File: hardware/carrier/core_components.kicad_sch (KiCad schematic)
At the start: 58 parts, among them J3 PANEL, J4 CARDKB, J6 EXT_LED, J7 HAPTIC, J8 PIEZ, M1 Walter, Q3 MMBT3904, Q4 AO3400A, Q5 UMH3N, SW2 SKQGAFE010, U11 SN74LVC2G126DCUR, U7 LIS2DW12TR, U8 CP2102N-A02-GQFN24, U9 DRV2605LDGSR

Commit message: Move sheets property to top level
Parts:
- removed C12, C13: 100uF, Capacitor_SMD:C_0805_2012Metric, symbol Device:C
- removed C14, C20, C22, C23: 10uF, Capacitor_SMD:C_0603_1608Metric, symbol Device:C
- removed C21, C24, C26, C29, C30, C32: 100nF, Capacitor_SMD:C_0603_1608Metric, symbol Device:C
- removed C25, C27: 1uF, Capacitor_SMD:C_0603_1608Metric, symbol Device:C
- removed C28, C31: 4.7uF, Capacitor_SMD:C_0603_1608Metric, symbol Device:C
- removed J3: PANEL, Connector_JST:JST_SH_SM10B-SRSS-TB_1x10-1MP_P1.00mm_Horizontal, symbol Connector_Generic:Conn_01x10
- removed J4: CARDKB, Connector_JST:JST_PH_S4B-PH-SM4-TB_1x04-1MP_P2.00mm_Horizontal, symbol Connector_Generic:Conn_01x04
- removed J6: EXT_LED, Connector_JST:JST_SH_SM02B-SRSS-TB_1x02-1MP_P1.00mm_Horizontal, symbol Connector_Generic:Conn_01x02
- removed J7: HAPTIC, Connector_JST:JST_SH_SM02B-SRSS-TB_1x02-1MP_P1.00mm_Horizontal, symbol Connector_Generic:Conn_01x02
- removed J8: PIEZ, Connector_JST:JST_SH_SM02B-SRSS-TB_1x02-1MP_P1.00mm_Horizontal, symbol Connector_Generic:Conn_01x02
- removed JP2: auto-boot, Jumper:SolderJumper-2_P1.3mm_Bridged_RoundedPad1.0x1.5mm, symbol Jumper:SolderJumper_2_Bridged
- removed M1: Walter, pager-carrier:Walter_Module_2x14_THT, symbol pager-carrier:Walter
- removed Q3: MMBT3904, Package_TO_SOT_SMD:SOT-23, symbol Transistor_BJT:MMBT3904
- removed Q4: AO3400A, Package_TO_SOT_SMD:SOT-23, symbol Transistor_FET:AO3400A
- removed Q5: UMH3N, Package_TO_SOT_SMD:SOT-363_SC-70-6, symbol Transistor_BJT:UMH3N
- removed R20: 0R, Resistor_SMD:R_0603_1608Metric, symbol Device:R
- removed R29, R30, R31, R32: 4.7k, Resistor_SMD:R_0603_1608Metric, symbol Device:R
- removed R33: 0R, Resistor_SMD:R_1206_3216Metric, symbol Device:R
- removed R34, R43: 1k, Resistor_SMD:R_0603_1608Metric, symbol Device:R
- removed R35, R36, R44, R45: 100k, Resistor_SMD:R_0603_1608Metric, symbol Device:R
- removed R37: 330R, Resistor_SMD:R_0603_1608Metric, symbol Device:R
- removed R38, R39: 220R, Resistor_SMD:R_0603_1608Metric, symbol Device:R
- removed R40: 15R, Resistor_SMD:R_0603_1608Metric, symbol Device:R
- removed R41: 22.1k, Resistor_SMD:R_0603_1608Metric, symbol Device:R
- removed R42: 47.5k, Resistor_SMD:R_0603_1608Metric, symbol Device:R
- removed R46, R47, R48: 10k, Resistor_SMD:R_0603_1608Metric, symbol Device:R
- removed R49: 1M, Resistor_SMD:R_0603_1608Metric, symbol Device:R
- removed SW2: SKQGAFE010, Button_Switch_SMD:SW_SPST_SKQG_WithoutStem, symbol Switch:SW_Push
- removed TP10: FL_BTN, TestPoint:TestPoint_Pad_1.0x1.0mm, symbol Connector:TestPoint
- removed TP11: 3V3_AWK, TestPoint:TestPoint_Pad_1.0x1.0mm, symbol Connector:TestPoint
- removed TP7: AWK_EN_N, TestPoint:TestPoint_Pad_1.0x1.0mm, symbol Connector:TestPoint
- removed TP8: TP_IO1, TestPoint:TestPoint_Pad_1.0x1.0mm, symbol Connector:TestPoint
- removed TP9: TP_IO5, TestPoint:TestPoint_Pad_1.0x1.0mm, symbol Connector:TestPoint
- removed U11: SN74LVC2G126DCUR, Package_SO:VSSOP-8_2.3x2mm_P0.5mm, symbol 74xGxx:74LVC2G126
- removed U7: LIS2DW12TR, Package_LGA:LGA-12_2x2mm_P0.5mm, symbol pager-carrier:LIS2DW12TR
- removed U8: CP2102N-A02-GQFN24, Package_DFN_QFN:QFN-24-1EP_4x4mm_P0.5mm_EP2.6x2.6mm, symbol Interface_USB:CP2102N-Axx-xQFN24
- removed U9: DRV2605LDGSR, Package_SO:TSSOP-10_3x3mm_P0.5mm, symbol pager-carrier:DRV2605LDGSR
- added C15, C16: 100uF, Capacitor_SMD:C_0805_2012Metric, symbol Device:C
- added C17, C38, C40, C43: 10uF, Capacitor_SMD:C_0603_1608Metric, symbol Device:C
- added C33, C36: 4.7uF, Capacitor_SMD:C_0603_1608Metric, symbol Device:C
- added C34, C35, C37, C39, C42, C45: 100nF, Capacitor_SMD:C_0603_1608Metric, symbol Device:C
- added C41, C44: 1uF, Capacitor_SMD:C_0603_1608Metric, symbol Device:C
- added J10: HAPTIC, Connector_JST:JST_SH_SM02B-SRSS-TB_1x02-1MP_P1.00mm_Horizontal, symbol Connector_Generic:Conn_01x02
- added J11: EXT_LED, Connector_JST:JST_SH_SM02B-SRSS-TB_1x02-1MP_P1.00mm_Horizontal, symbol Connector_Generic:Conn_01x02
- added J12: PIEZ, Connector_JST:JST_SH_SM02B-SRSS-TB_1x02-1MP_P1.00mm_Horizontal, symbol Connector_Generic:Conn_01x02
- added J5: PANEL, Connector_JST:JST_SH_SM10B-SRSS-TB_1x10-1MP_P1.00mm_Horizontal, symbol Connector_Generic:Conn_01x10
- added J9: CARDKB, Connector_JST:JST_PH_S4B-PH-SM4-TB_1x04-1MP_P2.00mm_Horizontal, symbol Connector_Generic:Conn_01x04
- added JP3: auto-boot, Jumper:SolderJumper-2_P1.3mm_Bridged_RoundedPad1.0x1.5mm, symbol Jumper:SolderJumper_2_Bridged
- added M2: Walter, pager-carrier:Walter_Module_2x14_THT, symbol pager-carrier:Walter
- added Q6: UMH3N, Package_TO_SOT_SMD:SOT-363_SC-70-6, symbol Transistor_BJT:UMH3N
- added Q7: AO3400A, Package_TO_SOT_SMD:SOT-23, symbol Transistor_FET:AO3400A
- added Q8: MMBT3904, Package_TO_SOT_SMD:SOT-23, symbol Transistor_BJT:MMBT3904
- added R21: 0R, Resistor_SMD:R_0603_1608Metric, symbol Device:R
- added R50: 22.1k, Resistor_SMD:R_0603_1608Metric, symbol Device:R
- added R51: 47.5k, Resistor_SMD:R_0603_1608Metric, symbol Device:R
- added R52, R58: 1k, Resistor_SMD:R_0603_1608Metric, symbol Device:R
- added R53, R54, R55, R59: 100k, Resistor_SMD:R_0603_1608Metric, symbol Device:R
- added R56, R57, R62: 10k, Resistor_SMD:R_0603_1608Metric, symbol Device:R
- added R60: 15R, Resistor_SMD:R_0603_1608Metric, symbol Device:R
- added R61: 0R, Resistor_SMD:R_1206_3216Metric, symbol Device:R
- added R63, R64, R65, R66: 4.7k, Resistor_SMD:R_0603_1608Metric, symbol Device:R
- added R67, R68: 220R, Resistor_SMD:R_0603_1608Metric, symbol Device:R
- added R69: 330R, Resistor_SMD:R_0603_1608Metric, symbol Device:R
- added R70: 1M, Resistor_SMD:R_0603_1608Metric, symbol Device:R
- added SW3: SKQGAFE010, Button_Switch_SMD:SW_SPST_SKQG_WithoutStem, symbol Switch:SW_Push
- added TP12: AWK_EN_N, TestPoint:TestPoint_Pad_1.0x1.0mm, symbol Connector:TestPoint
- added TP13: TP_IO1, TestPoint:TestPoint_Pad_1.0x1.0mm, symbol Connector:TestPoint
- added TP14: TP_IO5, TestPoint:TestPoint_Pad_1.0x1.0mm, symbol Connector:TestPoint
- added TP15: FL_BTN, TestPoint:TestPoint_Pad_1.0x1.0mm, symbol Connector:TestPoint
- added TP16: 3V3_AWK, TestPoint:TestPoint_Pad_1.0x1.0mm, symbol Connector:TestPoint
- added U12: CP2102N-A02-GQFN24, Package_DFN_QFN:QFN-24-1EP_4x4mm_P0.5mm_EP2.6x2.6mm, symbol Interface_USB:CP2102N-Axx-xQFN24
- added U13: SN74LVC2G126DCUR, Package_SO:VSSOP-8_2.3x2mm_P0.5mm, symbol 74xGxx:74LVC2G126
- added U14: DRV2605LDGSR, Package_SO:TSSOP-10_3x3mm_P0.5mm, symbol pager-carrier:DRV2605LDGSR
- added U15: LIS2DW12TR, Package_LGA:LGA-12_2x2mm_P0.5mm, symbol pager-carrier:LIS2DW12TR
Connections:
- net 3V3: now also C38.1, C42.1, C43.1, R21.1, R54.2, R62.2, R65.1, R66.1, U15.10 (VDD_IO), U15.2 (CS), U15.9 (VDD)
- net 3V3_AWK: now also C40.1, C44.1, C45.1, J9.3 (Pin_3), M2.26 (3V3_OUT), R63.1, R64.1, TP16.1, U14.10 (VDD), U14.5 (EN), U14.6 (VDD/NC)
- net ACC_INT1: now also M2.20 (IO16), U15.12 (INT1)
- net AON_SCL: now also M2.22 (IO18), R66.2, U15.1 (SCL/SPC)
- net AON_SDA: now also M2.21 (IO17), R65.2, U15.4 (SDA/SDI/SDO)
- net AWK_EN_N: now also JP3.2 (B), M2.4 (DFU/3V3_EN), TP12.1
- net AWK_SCL: now also J9.1 (Pin_1), M2.24 (IO9), R64.2, U14.2 (SCL)
- net AWK_SDA: now also J9.2 (Pin_2), M2.25 (IO10), R63.2, U14.3 (SDA)
- net BRG_3V3: now also C35.2, C36.2, C39.1, R52.2, U12.5 (VIO), U12.6 (VDD), U13.8 (VCC)
- net BRG_RXD: now also U12.20 (RXD), U13.6
- net BRG_TXD: now also U12.21 (TXD), U13.5
- net CHG_STAT1: now also M2.8 (IO38)
- net CHG_STAT2: now also M2.12 (IO42)
- net EINK_BUSY: now also J5.8 (Pin_8), M2.6 (IO11)
- net EINK_CS: now also J5.5 (Pin_5), M2.10 (IO40)
- net EINK_DC: now also J5.6 (Pin_6), M2.9 (IO39)
- net EINK_MOSI: now also J5.4 (Pin_4), M2.11 (IO41)
- net EINK_RST: now also J5.7 (Pin_7), M2.7 (IO13)
- net EINK_SCK: now also J5.3 (Pin_3), M2.13 (IO2)
- net ESP_EN: now also M2.1 (RESET), Q6.6 (C1)
- net ESP_RX0: now also M2.2 (IO44/RX0), R62.1, U13.3
- net ESP_TX0: now also M2.3 (IO43/TX0), U13.2
- net EXT_LED: now also M2.23 (IO8), R69.1
- net FL_BTN: now also C37.1, M2.15 (IO4), R54.1, SW3.1, TP15.1
- net FL_N: now also J5.10 (Pin_10), Q7.3 (D)
- net FL_P: now also J5.9 (Pin_9), R61.1
- net FL_PWM: now also M2.18 (IO7), R58.1
- net GND: now also C15.2, C16.2, C17.2, C33.2, C34.2, C35.1, C36.1, C37.2, C38.2, C39.2, C40.2, C41.2, C42.2, C43.2, C44.2, C45.2, J11.2 (Pin_2), J5.2 (Pin_2), J9.4 (Pin_4), M2.27 (GND), Q8.2 (E), R51.2, R53.2, R55.2, R59.2, R60.2, SW3.2, U12.18 (~{CTS}), U12.2 (GND), U12.25 (GND), U13.4 (GND), U14.4 (IN/TRIG), U14.8 (GND), U15.3 (SDO/SA0), U15.6 (GND), U15.7 (RES), U15.8 (GND)
- net PIEZ_N: now also M2.5 (IO12), R68.1
- net PIEZ_P: now also M2.17 (IO6), R67.1
- net SYS_SW: now also C15.1, C16.1, C17.1, M2.28 (VIN), R61.2
- net TP_IO1: now also M2.14 (IO1), TP13.1
- net TP_IO5: now also M2.16 (IO5), TP14.1
- net USB_DM: now also U12.4 (D-)
- net USB_DP: now also U12.3 (D+)
- net VBUS: now also C33.1, C34.1, R50.1, U12.7 (VREGIN)
- net VBUS_DET: now also M2.19 (IO15), U13.1, U13.7
- new net: J5.1 (Pin_1), R21.2
- new net: Q7.1 (G), Q8.3 (C), R58.2, R59.1
- new net: R50.2, R51.1, U12.8 (VBUS)
- new net: J12.1 (Pin_1), R67.2, R70.2
- new net: C41.1, U14.1 (REG)
- new net: JP3.1 (A), Q6.3 (C2)
- new net: Q6.4 (E2), R55.1, R56.1, U12.23 (~{DTR})
- new net: Q6.5 (B2), R57.2
- new net: J11.1 (Pin_1), R69.2
- new net: Q7.2 (S), Q8.1 (B), R60.1
- new net: Q6.1 (E1), R53.1, R57.1, U12.19 (~{RTS})
- new net: R52.1, U12.9 (~{RST})
- new net: J12.2 (Pin_2), R68.2, R70.1
- new net: J10.1 (Pin_1), U14.7 (OUT+)
- new net: J10.2 (Pin_2), U14.9 (OUT-)
- new net: Q6.2 (B1), R56.2
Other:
- company: awong-dev/pager -> (none)
- title: Walter module header, bulk capacitance, test pads, mounting holes -> (none)

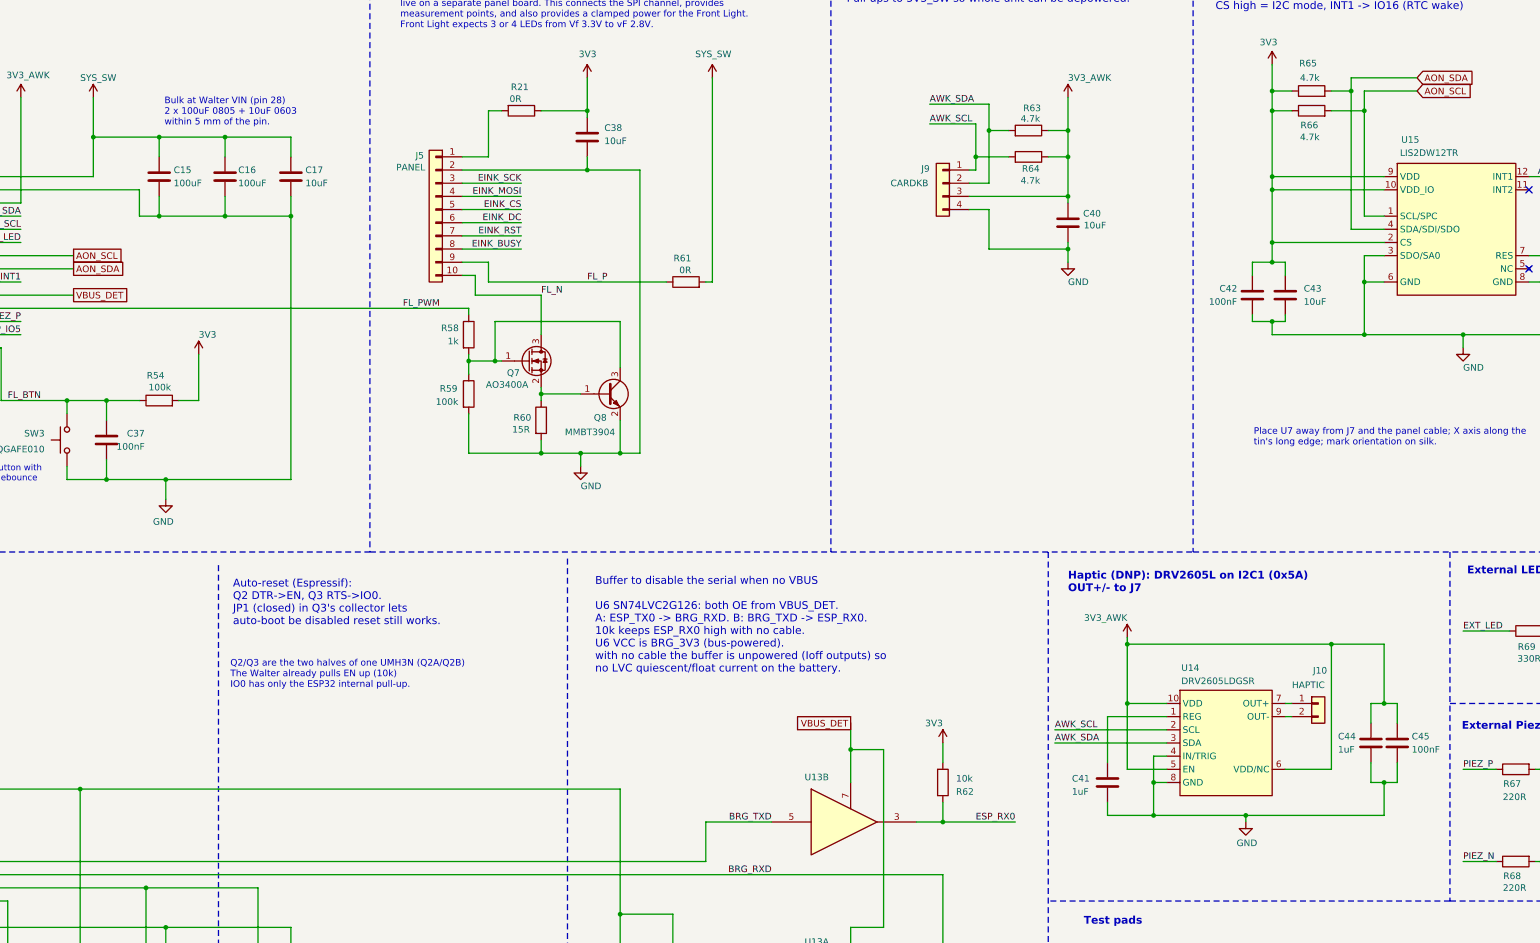
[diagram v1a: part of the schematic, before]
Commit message: Remove unnecessary caps and shrink some components
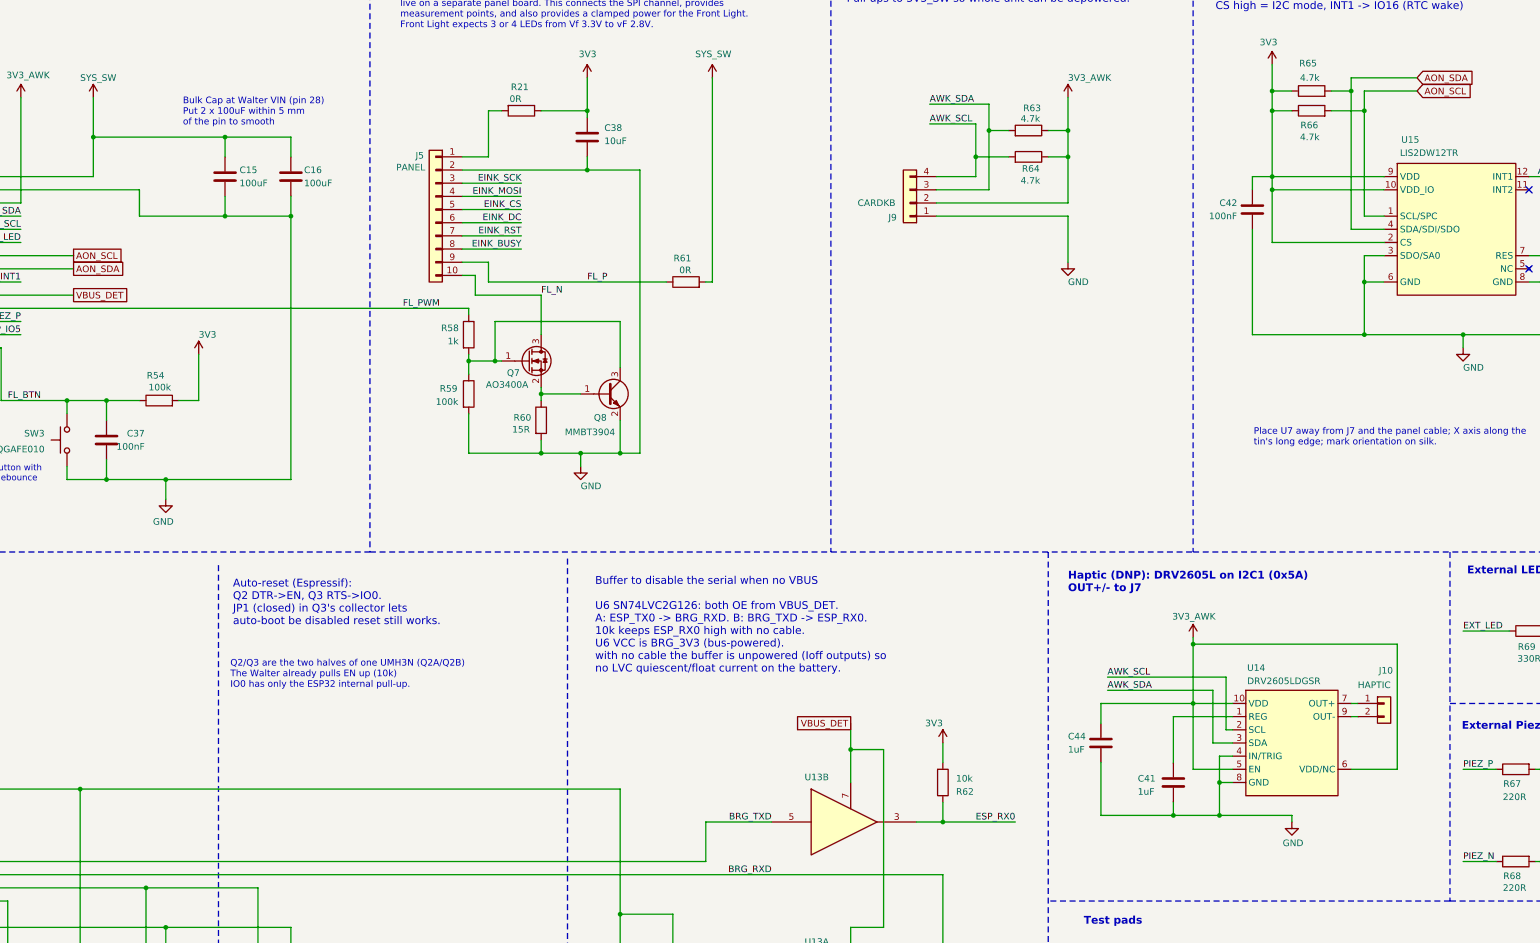
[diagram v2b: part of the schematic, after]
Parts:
- removed C17, C40, C43: 10uF, Capacitor_SMD:C_0603_1608Metric, symbol Device:C
- removed C45: 100nF, Capacitor_SMD:C_0603_1608Metric, symbol Device:C
- J9: footprint Connector_JST:JST_PH_S4B-PH-SM4-TB_1x04-1MP_P2.00mm_Horizontal -> Connector_JST:JST_SH_SM04B-SRSS-TB_1x04-1MP_P1.00mm_Horizontal
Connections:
- net 3V3_AWK: now also J9.2 (Pin_2); no longer J9.3 (Pin_3)
- net AWK_SCL: now also J9.4 (Pin_4); no longer J9.1 (Pin_1)
- net AWK_SDA: now also J9.3 (Pin_3); no longer J9.2 (Pin_2)
- net GND: now also J9.1 (Pin_1); no longer J9.4 (Pin_4)
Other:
- note added: "Bulk Cap at Walter VIN (pin 28) Put 2 x 100uF within 5 mm of the pin to smooth"
- note removed: "Bulk at Walter VIN (pin 28) 2 x 100uF 0805 + 10uF 0603 within 5 mm of the pin."
- moved on the sheet: C15, C16, C41, C42, C44, J10, J9, U14

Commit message: AI resized many of the components
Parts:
- C34, C35, C37, C39, C42: footprint Capacitor_SMD:C_0603_1608Metric -> Capacitor_SMD:C_0402_1005Metric; LCSC C14663 -> C1525; MPN CL10B104KB8NNNC -> CL05B104KO5NNNC
- C36: footprint Capacitor_SMD:C_0603_1608Metric -> Capacitor_SMD:C_0402_1005Metric; LCSC C19666 -> C23733; MPN CL10A475KP8NNNC -> CL05A475MP5NRNC
- C41, C44: footprint Capacitor_SMD:C_0603_1608Metric -> Capacitor_SMD:C_0402_1005Metric; LCSC C15849 -> C52923; MPN CL10A105KA8NNNC -> CL05A105KA5NQNC
- Q7: value AO3400A -> SI1308EDL; footprint Package_TO_SOT_SMD:SOT-23 -> Package_TO_SOT_SMD:SOT-323_SC-70; LCSC C20917 -> C469327; MPN AO3400A -> SI1308EDL-T1-GE3
- Q8: value MMBT3904 -> MMST3904; footprint Package_TO_SOT_SMD:SOT-23 -> Package_TO_SOT_SMD:SOT-323_SC-70; LCSC C20526 -> C54879; MPN MMBT3904 -> MMST3904
- R21: footprint Resistor_SMD:R_0603_1608Metric -> Resistor_SMD:R_0402_1005Metric; LCSC C21189 -> C17168; MPN 0603WAF0000T5E -> 0402WGF0000TCE
- R50: footprint Resistor_SMD:R_0603_1608Metric -> Resistor_SMD:R_0402_1005Metric; LCSC C137768 -> C43473; MPN RC0603FR-0722K1L -> 0402WGF2212TCE
- R51: footprint Resistor_SMD:R_0603_1608Metric -> Resistor_SMD:R_0402_1005Metric; LCSC C23061 -> C25896; MPN 0603WAF4752T5E -> 0402WGF4752TCE
- R52, R58: footprint Resistor_SMD:R_0603_1608Metric -> Resistor_SMD:R_0402_1005Metric; LCSC C21190 -> C11702; MPN 0603WAF1001T5E -> 0402WGF1001TCE
- R53, R54, R55, R59: footprint Resistor_SMD:R_0603_1608Metric -> Resistor_SMD:R_0402_1005Metric; LCSC C25803 -> C25741; MPN 0603WAF1003T5E -> 0402WGF1003TCE
- R56, R57, R62: footprint Resistor_SMD:R_0603_1608Metric -> Resistor_SMD:R_0402_1005Metric; LCSC C25804 -> C25744; MPN 0603WAF1002T5E -> 0402WGF1002TCE
- R61: footprint Resistor_SMD:R_1206_3216Metric -> Resistor_SMD:R_0402_1005Metric; LCSC C17888 -> C17168; MPN 1206W4F0000T5E -> 0402WGF0000TCE
- R63, R64, R65, R66: footprint Resistor_SMD:R_0603_1608Metric -> Resistor_SMD:R_0402_1005Metric; LCSC C23162 -> C25900; MPN 0603WAF4701T5E -> 0402WGF4701TCE
- R67, R68: footprint Resistor_SMD:R_0603_1608Metric -> Resistor_SMD:R_0402_1005Metric; LCSC C22962 -> C25091; MPN 0603WAF2200T5E -> 0402WGF2200TCE
- R69: footprint Resistor_SMD:R_0603_1608Metric -> Resistor_SMD:R_0402_1005Metric; LCSC C23138 -> C25104; MPN 0603WAF3300T5E -> 0402WGF3300TCE
- R70: footprint Resistor_SMD:R_0603_1608Metric -> Resistor_SMD:R_0402_1005Metric; LCSC C22935 -> C26083; MPN 0603WAF1004T5E -> 0402WGF1004TCE

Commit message: components renumbered
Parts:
- renumbered C33 to C1, C44 to C10, C41 to C11, C42 to C12, C34 to C2, C35 to C3, C36 to C4, C37 to C5, C15 to C6, C16 to C7, C38 to C8, C39 to C9, J5 to J1, J9 to J2, J10 to J3, J11 to J4, J12 to J5, JP3 to JP1, M2 to M1, Q6 to Q1, Q7 to Q2, Q8 to Q3, R50 to R1, R59 to R10, R21 to R11, R60 to R12, R61 to R13, R62 to R14, R63 to R15, R64 to R16, R65 to R17, R66 to R18, R67 to R19, R51 to R2, R68 to R20, R69 to R21, R70 to R22, R52 to R3, R53 to R4, R54 to R5, R55 to R6, R56 to R7, R57 to R8, R58 to R9, SW3 to SW1, TP12 to TP1, TP13 to TP2, TP14 to TP3, TP15 to TP4, TP16 to TP5, U12 to U1, U13 to U2, U14 to U3, U15 to U4

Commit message: Attempt to layout the PCB
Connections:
- net 3V3_J1: now reaches J1.1 (Pin_1), R11.2
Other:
- moved on the sheet: C8, J1, Q2, Q3, R10, R11, R12, R13, R9
